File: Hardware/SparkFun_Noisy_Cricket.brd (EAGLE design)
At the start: 31.8 x 25.4 mm, 29 parts, among them U1 LM4853

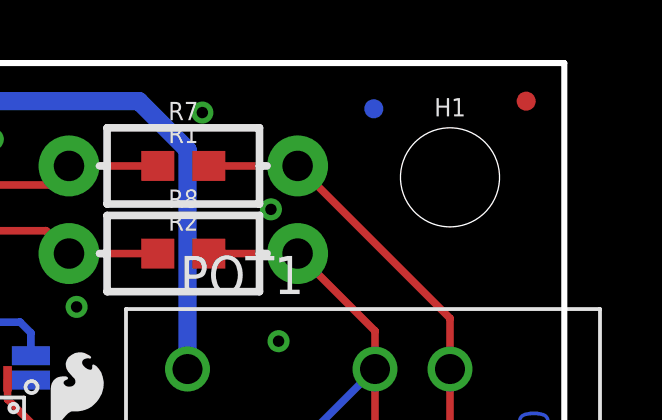
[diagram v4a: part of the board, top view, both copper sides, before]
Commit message: Design Review Changes
minor changes to silk after design review
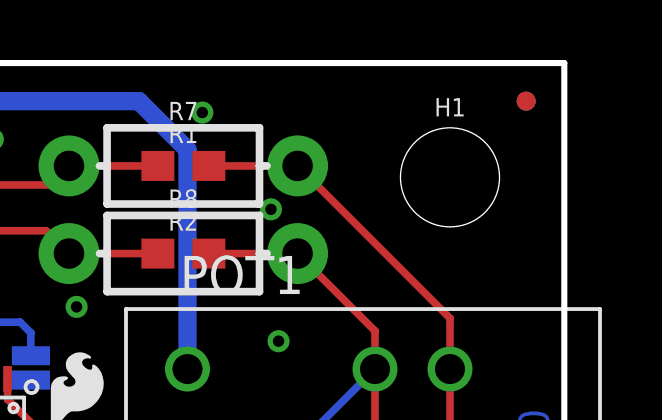
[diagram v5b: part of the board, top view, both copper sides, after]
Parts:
- moved FD4 5.09 mm to (30.5, 24.1)
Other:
- board text added: "ENABLE MONO OUTPUT"
- board text removed: "MONO OUTPUT"
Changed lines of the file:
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@@
 <layer number="20" name="Dimension" color="15" fill="1" visible="yes" active="yes"/>
 <layer number="21" name="tPlace" color="16" fill="1" visible="yes" active="yes"/>
-<layer number="22" name="bPlace" color="14" fill="1" visible="yes" active="yes"/>
+<layer number="22" name="bPlace" color="14" fill="1" visible="no" active="yes"/>
 <layer number="23" name="tOrigins" color="15" fill="1" visible="yes" active="yes"/>
-<layer number="24" name="bOrigins" color="15" fill="1" visible="yes" active="yes"/>
+<layer number="24" name="bOrigins" color="15" fill="1" visible="no" active="yes"/>
 <layer number="25" name="tNames" color="7" fill="1" visible="no" active="yes"/>
 <layer number="26" name="bNames" color="7" fill="1" visible="no" active="yes"/>
@@
 <layer number="37" name="tTest" color="7" fill="1" visible="no" active="yes"/>
 <layer number="38" name="bTest" color="7" fill="1" visible="no" active="yes"/>
-<layer number="39" name="tKeepout" color="4" fill="11" visible="no" active="yes"/>
-<layer number="40" name="bKeepout" color="1" fill="11" visible="no" active="yes"/>
+<layer number="39" name="tKeepout" color="4" fill="11" visible="yes" active="yes"/>
+<layer number="40" name="bKeepout" color="1" fill="11" visible="yes" active="yes"/>
 <layer number="41" name="tRestrict" color="4" fill="10" visible="no" active="yes"/>
 <layer number="42" name="bRestrict" color="1" fill="10" visible="no" active="yes"/>
 <layer number="43" name="vRestrict" color="2" fill="10" visible="no" active="yes"/>
 <layer number="44" name="Drills" color="7" fill="1" visible="no" active="yes"/>
-<layer number="45" name="Holes" color="7" fill="1" visible="yes" active="yes"/>
+<layer number="45" name="Holes" color="7" fill="1" visible="no" active="yes"/>
 <layer number="46" name="Milling" color="3" fill="1" visible="no" active="yes"/>
-<layer number="47" name="Measures" color="7" fill="1" visible="no" active="yes"/>
+<layer number="47" name="Measures" color="7" fill="1" visible="yes" active="yes"/>
 <layer number="48" name="Document" color="7" fill="1" visible="no" active="yes"/>
 <layer number="49" name="Reference" color="7" fill="1" visible="no" active="yes"/>
@@
 <text x="2.54" y="3.81" size="0.8128" layer="22" font="vector" ratio="15" rot="MR180" align="center-left">GND</text>
 <text x="2.54" y="1.27" size="0.8128" layer="22" font="vector" ratio="15" rot="MR180" align="center-left">MONO</text>
-<text x="13.97" y="12.954" size="0.8128" layer="22" font="vector" ratio="15" rot="MR180" align="center">MONO
+<text x="13.97" y="12.446" size="0.8128" layer="22" font="vector" ratio="15" rot="MR180" align="center">ENABLE
+MONO
 OUTPUT</text>
 <dimension x1="0" y1="0" x2="0" y2="25.4" x3="-5.08" y3="12.7" textsize="1.27" textratio="15" layer="47" unit="inch"/>
@@
 <element name="FD2" library="SparkFun-Aesthetics" package="FIDUCIAL-MICRO" value="FIDUCIALUFIDUCIAL" x="30.48" y="24.13"/>
 <element name="FD3" library="SparkFun-Aesthetics" package="FIDUCIAL-MICRO" value="FIDUCIALUFIDUCIAL" x="2.159" y="2.54" rot="MR0"/>
-<element name="FD4" library="SparkFun-Aesthetics" package="FIDUCIAL-MICRO" value="FIDUCIALUFIDUCIAL" x="25.4" y="23.876" rot="MR0"/>
+<element name="FD4" library="SparkFun-Aesthetics" package="FIDUCIAL-MICRO" value="FIDUCIALUFIDUCIAL" x="30.48" y="24.13" rot="MR0"/>
 <element name="H1" library="SparkFun-Hardware" package="STAND-OFF" value="STAND-OFF" x="27.94" y="21.59"/>
 <element name="H2" library="SparkFun-Hardware" package="STAND-OFF" value="STAND-OFF" x="27.94" y="3.81"/>

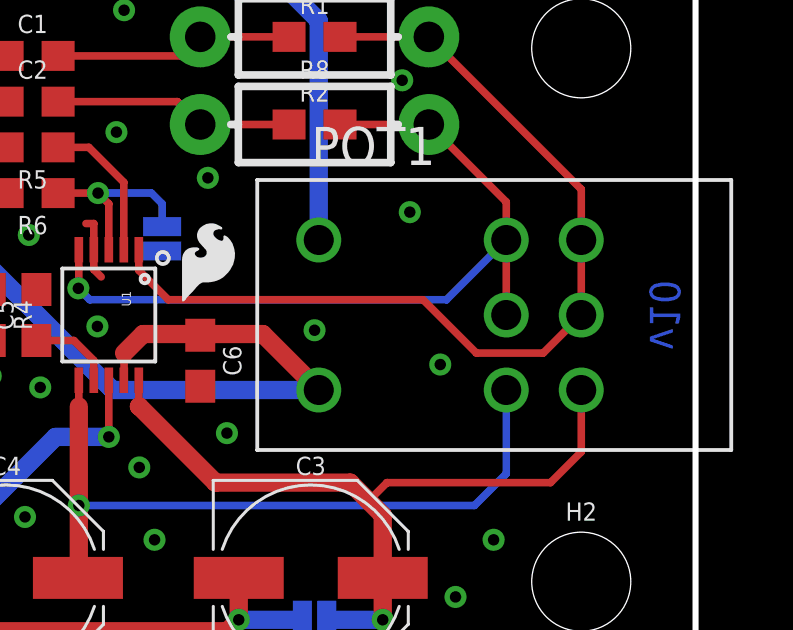
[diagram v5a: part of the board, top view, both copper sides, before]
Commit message: QC Fixes
- Increased anular ring of pot from AUTO to 0.074".
- Fixed schematic version number to 10.
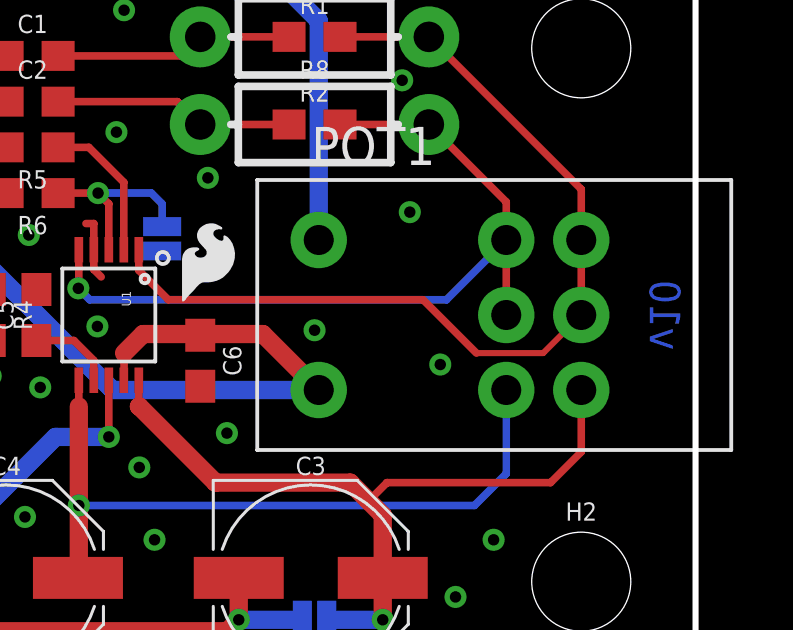
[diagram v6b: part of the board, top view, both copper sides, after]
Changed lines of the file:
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@@
 <layer number="20" name="Dimension" color="15" fill="1" visible="yes" active="yes"/>
 <layer number="21" name="tPlace" color="16" fill="1" visible="yes" active="yes"/>
-<layer number="22" name="bPlace" color="14" fill="1" visible="no" active="yes"/>
+<layer number="22" name="bPlace" color="14" fill="1" visible="yes" active="yes"/>
 <layer number="23" name="tOrigins" color="15" fill="1" visible="yes" active="yes"/>
-<layer number="24" name="bOrigins" color="15" fill="1" visible="no" active="yes"/>
+<layer number="24" name="bOrigins" color="15" fill="1" visible="yes" active="yes"/>
 <layer number="25" name="tNames" color="7" fill="1" visible="no" active="yes"/>
 <layer number="26" name="bNames" color="7" fill="1" visible="no" active="yes"/>
@@
 <layer number="37" name="tTest" color="7" fill="1" visible="no" active="yes"/>
 <layer number="38" name="bTest" color="7" fill="1" visible="no" active="yes"/>
-<layer number="39" name="tKeepout" color="4" fill="11" visible="yes" active="yes"/>
-<layer number="40" name="bKeepout" color="1" fill="11" visible="yes" active="yes"/>
+<layer number="39" name="tKeepout" color="4" fill="11" visible="no" active="yes"/>
+<layer number="40" name="bKeepout" color="1" fill="11" visible="no" active="yes"/>
 <layer number="41" name="tRestrict" color="4" fill="10" visible="no" active="yes"/>
 <layer number="42" name="bRestrict" color="1" fill="10" visible="no" active="yes"/>
 <layer number="43" name="vRestrict" color="2" fill="10" visible="no" active="yes"/>
 <layer number="44" name="Drills" color="7" fill="1" visible="no" active="yes"/>
-<layer number="45" name="Holes" color="7" fill="1" visible="no" active="yes"/>
+<layer number="45" name="Holes" color="7" fill="1" visible="yes" active="yes"/>
 <layer number="46" name="Milling" color="3" fill="1" visible="no" active="yes"/>
-<layer number="47" name="Measures" color="7" fill="1" visible="yes" active="yes"/>
+<layer number="47" name="Measures" color="7" fill="1" visible="no" active="yes"/>
 <layer number="48" name="Document" color="7" fill="1" visible="no" active="yes"/>
 <layer number="49" name="Reference" color="7" fill="1" visible="no" active="yes"/>
@@
 <wire x1="13.192" y1="14.189928125" x2="13.192" y2="14.875" width="0.254" layer="1"/>
 <wire x1="22.667628125" y1="13.208" x2="24.445628125" y2="11.43" width="0.254" layer="1"/>
-<wire x1="24.445628125" y1="11.43" x2="26.67" y2="11.43" width="0.254" layer="1"/>
-<wire x1="26.67" y1="11.43" x2="27.94" y2="12.7" width="0.254" layer="1"/>
+<wire x1="24.445628125" y1="11.43" x2="26.67" y2="11.43" width="0.2032" layer="1"/>
+<wire x1="26.67" y1="11.43" x2="27.94" y2="12.7" width="0.2032" layer="1"/>
 <wire x1="22.86" y1="21.971" x2="27.94" y2="16.891" width="0.254" layer="1"/>
 <wire x1="27.94" y1="16.891" x2="27.94" y2="15.2" width="0.254" layer="1"/>
